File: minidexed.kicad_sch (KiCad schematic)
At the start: 50 parts, among them J1 AudioJack3, J2 AudioJack3, J3 AudioJack3, J4 AudioJack3, J5 Raspberry_Pi_2_3, SW1 SW_Push, SW2 SW_Push, SW3 SW_Push, SW4 Encoder, U1 A3.3V ME6211C33, U2 D3.3V ME6211C33, U3 74HCT14, U4 PCM5102, U5 6N138

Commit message: pre-tracks
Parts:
- removed C11, C12: 10, symbol Device:C
- removed C14, C15, C6: 0.1, symbol Device:C
- removed D1: 1N4148, Diode_THT:D_DO-35_SOD27_P7.62mm_Horizontal, symbol Diode:1N4148
- removed J1, J3: AudioJack3, symbol Connector:AudioJack3
- removed R6: 220, symbol Device:R
- removed R7: 3K3, symbol Device:R
- removed U2: D3.3V ME6211C33, Package_TO_SOT_SMD:TSOT-23-5, symbol Regulator_Linear:ADP7142AUJZ
- removed U5: 6N138, symbol Isolator:6N138
- added C13: 10uf, Capacitor_SMD:C_0805_2012Metric_Pad1.18x1.45mm_HandSolder, symbol Device:C
- added C7, C9: 100nf, Capacitor_SMD:C_0805_2012Metric_Pad1.18x1.45mm_HandSolder, symbol Device:C
- added D1: 1N4148WS, Diode_SMD:D_SOD-323, symbol Diode:1N4148WS
- added H1, H2, H3: MountingHole, MountingHole:MountingHole_2.7mm_M2.5, symbol Mechanical:MountingHole
- added J4: MIDI Thru, sparkfun 3.5mm:sparkfun_3.5mm_trs, symbol Connector:AudioJack3
- added J5: MIDI Out, sparkfun 3.5mm:sparkfun_3.5mm_trs, symbol Connector:AudioJack3
- added J6: GND TP, Connector_PinHeader_2.54mm:PinHeader_1x02_P2.54mm_Vertical, symbol Connector:Conn_01x02_Male
- added R12: 470, Resistor_SMD:R_1206_3216Metric_Pad1.30x1.75mm_HandSolder, symbol Device:R
- added TP5: 5V Analog DAC, TestPoint:TestPoint_Pad_D1.0mm, symbol Connector:TestPoint
- added TP6: 3.3V Analog DAC, TestPoint:TestPoint_Pad_D1.0mm, symbol Connector:TestPoint
- added TP8: 3.3V Digital DAC, TestPoint:TestPoint_Pad_D1.0mm, symbol Connector:TestPoint
- added U4: H11L1, Package_SO:TSOP-6_1.65x3.05mm_P0.95mm, symbol Isolator:H11L1
- C1, C5: value 0.1 -> 100nf; footprint (none) -> Capacitor_SMD:C_0805_2012Metric_Pad1.18x1.45mm_HandSolder; LCSC (none) -> C472810
- C10: value 10n -> 10uf; footprint (none) -> Capacitor_SMD:C_0805_2012Metric_Pad1.18x1.45mm_HandSolder; LCSC (none) -> C111662
- C11: renamed from C17; footprint (none) -> Capacitor_SMD:C_0805_2012Metric_Pad1.18x1.45mm_HandSolder; LCSC (none) -> C77455
- C12: renamed from C18; footprint (none) -> Capacitor_SMD:C_0805_2012Metric_Pad1.18x1.45mm_HandSolder; LCSC (none) -> C77455
- C14: renamed from C13; value 2.2 -> 2.2nf; footprint (none) -> Capacitor_SMD:C_0805_2012Metric_Pad1.18x1.45mm_HandSolder; LCSC (none) -> C395967
- C15: renamed from C16; value 2.2 -> 2.2nf; footprint (none) -> Capacitor_SMD:C_0805_2012Metric_Pad1.18x1.45mm_HandSolder; LCSC (none) -> C395967
- C16: renamed from C7; value 10n -> 0.1uf; footprint (none) -> Capacitor_SMD:C_0805_2012Metric_Pad1.18x1.45mm_HandSolder
- C2: value 0.1 -> 10uf; footprint (none) -> Capacitor_SMD:C_0805_2012Metric_Pad1.18x1.45mm_HandSolder; LCSC (none) -> C111662
- C3: value 10 -> 100nf; footprint (none) -> Capacitor_SMD:C_0805_2012Metric_Pad1.18x1.45mm_HandSolder; LCSC (none) -> C472810
- C4: value 10 -> 10uf; footprint (none) -> Capacitor_SMD:C_0805_2012Metric_Pad1.18x1.45mm_HandSolder; LCSC (none) -> C111662
- C6: renamed from C8; value 2.2 -> 2.2uf; footprint (none) -> Capacitor_SMD:C_0805_2012Metric_Pad1.18x1.45mm_HandSolder; LCSC (none) -> C6119894
- C8: renamed from C9; value 2.2 -> 2.2uf; footprint (none) -> Capacitor_SMD:C_0805_2012Metric_Pad1.18x1.45mm_HandSolder; LCSC (none) -> C6119894
- J1: renamed from J4; value AudioJack3 -> Audio Out; footprint (none) -> sparkfun 3.5mm:sparkfun_3.5mm_trs
- J2: value AudioJack3 -> MIDI In; footprint (none) -> sparkfun 3.5mm:sparkfun_3.5mm_trs
- J3: renamed from J5; footprint (none) -> raspberry-pi_rpi_hat:raspberry-pi_rpi_hat
- R1: renamed from R2; footprint (none) -> Resistor_SMD:R_1206_3216Metric_Pad1.30x1.75mm_HandSolder; LCSC (none) -> C104814
- R10: renamed from R4; footprint (none) -> Resistor_SMD:R_1206_3216Metric_Pad1.30x1.75mm_HandSolder; LCSC (none) -> C872616
- R11: renamed from R5; footprint (none) -> Resistor_SMD:R_1206_3216Metric_Pad1.30x1.75mm_HandSolder; LCSC (none) -> C872616
- R13: renamed from R8; footprint (none) -> Resistor_SMD:R_1206_3216Metric_Pad1.30x1.75mm_HandSolder; LCSC (none) -> C872616
- R14: renamed from R9; footprint (none) -> Resistor_SMD:R_1206_3216Metric_Pad1.30x1.75mm_HandSolder; LCSC (none) -> C872616
- R2: renamed from R10; footprint (none) -> Resistor_SMD:R_1206_3216Metric_Pad1.30x1.75mm_HandSolder; LCSC (none) -> C237143
- R3: renamed from R11; footprint (none) -> Resistor_SMD:R_1206_3216Metric_Pad1.30x1.75mm_HandSolder; LCSC (none) -> C237143
- R4: renamed from R3; footprint (none) -> Resistor_SMD:R_1206_3216Metric_Pad1.30x1.75mm_HandSolder; LCSC (none) -> C104814
- R5: renamed from R12; footprint (none) -> Resistor_SMD:R_1206_3216Metric_Pad1.30x1.75mm_HandSolder; LCSC (none) -> C237143
- R6: renamed from R1; footprint (none) -> Resistor_SMD:R_1206_3216Metric_Pad1.30x1.75mm_HandSolder; LCSC (none) -> C872616
- R7: renamed from R13; footprint (none) -> Resistor_SMD:R_1206_3216Metric_Pad1.30x1.75mm_HandSolder; LCSC (none) -> C912903
- R8: renamed from R14; footprint (none) -> Resistor_SMD:R_1206_3216Metric_Pad1.30x1.75mm_HandSolder; LCSC (none) -> C912903
- R9: renamed from R15; footprint (none) -> Resistor_SMD:R_1206_3216Metric_Pad1.30x1.75mm_HandSolder; LCSC (none) -> C912903
- RV1: value R_Potentiometer -> 10k; footprint (none) -> Potentiometer_THT:Potentiometer_Runtron_RM-065_Vertical
- SW1: renamed from SW4; footprint (none) -> Rotary_Encoder:RotaryEncoder_Alps_EC11E-Switch_Vertical_H20mm
- SW2: renamed from SW1; value SW_Push -> B1; footprint (none) -> Button_Switch_Keyboard:SW_Cherry_MX_1.00u_PCB
- SW3: renamed from SW2; value SW_Push -> B2; footprint (none) -> Button_Switch_Keyboard:SW_Cherry_MX_1.00u_PCB
- SW4: renamed from SW3; value SW_Push -> B3; footprint (none) -> Button_Switch_Keyboard:SW_Cherry_MX_1.00u_PCB
- U1: LCSC (none) -> C82942
- U2: renamed from U4; LCSC (none) -> C107671
- U3: footprint (none) -> Package_SO:TSSOP-14_4.4x3.6mm_P0.4mm; LCSC (none) -> C133639
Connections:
- net DAC_D_3V3 is gone; now on net +3.3V: C4.1, U2.17 (XSMT), U2.20 (DVDD)
- net +3.3V: now also C5.1, R12.1, TP8.1, U4.6; no longer C10.1
- net +5V: now also TP5.1; no longer C2.1
- net DAC_A_3V3: now also C10.1, C2.1, C7.1, TP6.1; no longer C5.1
- net GND: now also C6.2, J1.1 (S), U2.3 (CPGND), C13.2, C7.2, C9.2, J4.1 (S), J5.1 (S), J6.1 (Pin_1), J6.2 (Pin_2), U4.5; no longer J1.S, J2.S
- net MIDI_RX: now also R12.2, U4.4
- net at R13.1: now also J4.2 (R); no longer J2.R
- net at R10.1: now also J4.5 (T); no longer J2.T
- net at C14.1, R1.2: now also J1.5 (T); no longer J1.T
- net at R14.1: now also J5.2 (R)
- net at R6.2: now also D1.1 (K), U4.1
- net at U2.18 (LDOO): now also C13.1, C9.1
- net at R6.1: now also J2.2 (R)
- net at C15.1, R4.2: now also J1.2 (R); no longer J1.R
- net at R11.1: now also J5.5 (T)
- new net: D1.2 (A), J2.5 (T), U4.2
- no-connect marks 20 -> 19
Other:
- removed sheet DAC
- removed sheet MIDI IO
- note added: "BUTTONS"
- note added: "DAC"
- note added: "ENCODER"
- note added: "I don't think an optocoupler needs a bypass cap?"
- note added: "Is this overkill using a regulator when we already have 3.3V available?"
- note added: "MIDI"
- note added: "RPI"
- note removed: "INTERFACE"
- note removed: "MIDI IN"
- note removed: "MIDI OUT"
- note removed: "MIDI THRU"
- note removed: "Questions: - Analog vs digital ground"
- moved on the sheet: C1, C11, C12, C14, C15, C16, C6, C8, DS1, J3, R1, R10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

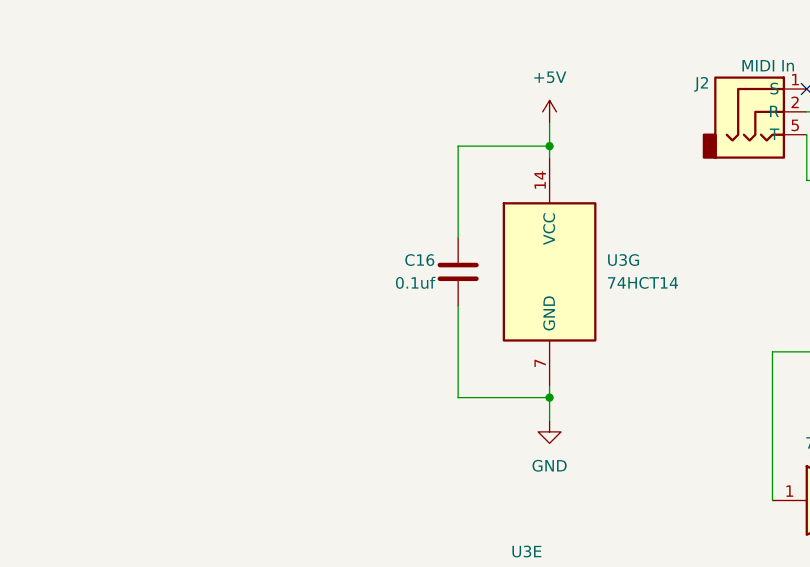
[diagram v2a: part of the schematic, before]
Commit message: update opto footprint
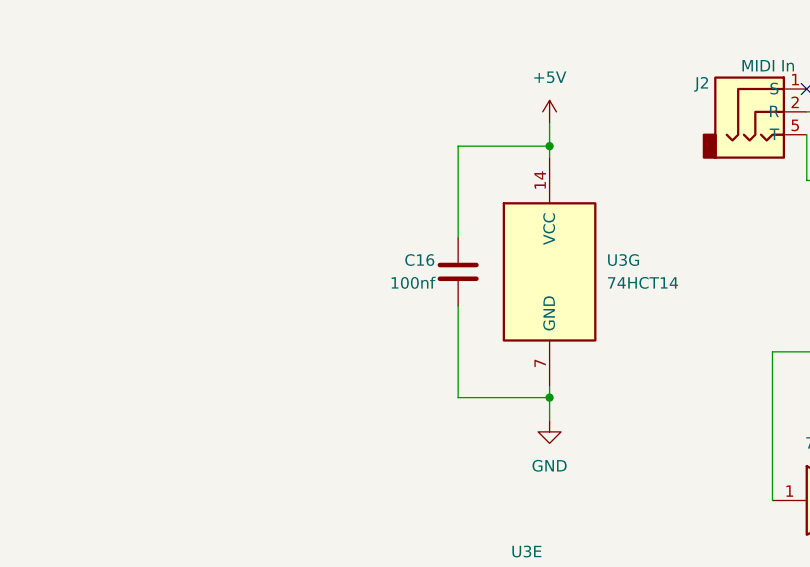
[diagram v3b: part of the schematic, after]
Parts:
- C16: value 0.1uf -> 100nf; LCSC (none) -> C472810
- R2, R3, R5: LCSC C237143 -> C2073539
- U3: footprint Package_SO:TSSOP-14_4.4x3.6mm_P0.4mm -> Package_SO:TSSOP-14_4.4x5mm_P0.65mm
- U4: footprint Package_SO:TSOP-6_1.65x3.05mm_P0.95mm -> SOP-6_6.5x7.12mm_P2.54mm:SOP-6_6.5x7.12mm_P2.54mm
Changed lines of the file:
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@@
     (property "Reference" "U4" (id 0) (at 420.37 242.57 0))
     (property "Value" "H11L1" (id 1) (at 421.64 245.11 0))
-    (property "Footprint" "Package_SO:TSOP-6_1.65x3.05mm_P0.95mm" (id 2) (at 410.464 240.03 0)
+    (property "Footprint" "SOP-6_6.5x7.12mm_P2.54mm:SOP-6_6.5x7.12mm_P2.54mm" (id 2) (at 410.464 240.03 0)
       (effects (font (size 1.27 1.27)) hide)
     )
@@
     (property "Reference" "U3" (id 0) (at 408.94 271.78 0))
     (property "Value" "74HCT14" (id 1) (at 408.94 274.32 0))
-    (property "Footprint" "Package_SO:TSSOP-14_4.4x3.6mm_P0.4mm" (id 2) (at 408.94 280.67 0)
+    (property "Footprint" "Package_SO:TSSOP-14_4.4x5mm_P0.65mm" (id 2) (at 408.94 280.67 0)
       (effects (font (size 1.27 1.27)) hide)
     )
@@
       (effects (font (size 1.27 1.27)) hide)
     )
-    (property "LCSC" "C237143" (id 4) (at 239.395 72.39 0)
+    (property "LCSC" "C2073539" (id 4) (at 239.395 72.39 0)
       (effects (font (size 1.27 1.27)) hide)
     )
@@
     (property "Reference" "U3" (id 0) (at 388.62 271.78 0))
     (property "Value" "74HCT14" (id 1) (at 388.62 274.32 0))
-    (property "Footprint" "Package_SO:TSSOP-14_4.4x3.6mm_P0.4mm" (id 2) (at 388.62 280.67 0)
+    (property "Footprint" "Package_SO:TSSOP-14_4.4x5mm_P0.65mm" (id 2) (at 388.62 280.67 0)
       (effects (font (size 1.27 1.27)) hide)
     )
@@
       (effects (font (size 1.27 1.27)) hide)
     )
-    (property "LCSC" "C237143" (id 4) (at 273.685 78.74 0)
+    (property "LCSC" "C2073539" (id 4) (at 273.685 78.74 0)
       (effects (font (size 1.27 1.27)) hide)
     )
@@
       (effects (font (size 1.27 1.27)) hide)
     )
-    (property "LCSC" "C237143" (id 4) (at 239.395 96.52 0)
+    (property "LCSC" "C2073539" (id 4) (at 239.395 96.52 0)
       (effects (font (size 1.27 1.27)) hide)
     )
@@
       (effects (font (size 1.27 1.27)) (justify left))
     )
-    (property "Footprint" "Package_SO:TSSOP-14_4.4x3.6mm_P0.4mm" (id 2) (at 356.235 255.27 0)
+    (property "Footprint" "Package_SO:TSSOP-14_4.4x5mm_P0.65mm" (id 2) (at 356.235 255.27 0)
       (effects (font (size 1.27 1.27)) hide)
     )
@@
     (property "Reference" "U3" (id 0) (at 353.695 301.625 0))
     (property "Value" "74HCT14" (id 1) (at 353.695 304.165 0))
-    (property "Footprint" "Package_SO:TSSOP-14_4.4x3.6mm_P0.4mm" (id 2) (at 353.695 310.515 0)
+    (property "Footprint" "Package_SO:TSSOP-14_4.4x5mm_P0.65mm" (id 2) (at 353.695 310.515 0)
       (effects (font (size 1.27 1.27)) hide)
     )
@@
       (effects (font (size 1.27 1.27)) (justify left))
     )
-    (property "Value" "0.1uf" (id 1) (at 343.535 256.54 0)
+    (property "Value" "100nf" (id 1) (at 343.535 256.54 0)
       (effects (font (size 1.27 1.27)) (justify left))
     )
@@
     )
     (property "Datasheet" "~" (id 3) (at 346.075 255.27 0)
+      (effects (font (size 1.27 1.27)) hide)
+    )
+    (property "LCSC" "C472810" (id 4) (at 346.075 255.27 0)
       (effects (font (size 1.27 1.27)) hide)
     )
@@
     (property "Reference" "U3" (id 0) (at 388.62 294.64 0))
     (property "Value" "74HCT14" (id 1) (at 388.62 297.18 0))
-    (property "Footprint" "Package_SO:TSSOP-14_4.4x3.6mm_P0.4mm" (id 2) (at 388.62 303.53 0)
+    (property "Footprint" "Package_SO:TSSOP-14_4.4x5mm_P0.65mm" (id 2) (at 388.62 303.53 0)
       (effects (font (size 1.27 1.27)) hide)
     )
@@
     (property "Reference" "U3" (id 0) (at 353.695 286.385 0))
     (property "Value" "74HCT14" (id 1) (at 353.695 288.925 0))
-    (property "Footprint" "Package_SO:TSSOP-14_4.4x3.6mm_P0.4mm" (id 2) (at 353.695 295.275 0)
+    (property "Footprint" "Package_SO:TSSOP-14_4.4x5mm_P0.65mm" (id 2) (at 353.695 295.275 0)
       (effects (font (size 1.27 1.27)) hide)
     )
@@
     (property "Reference" "U3" (id 0) (at 408.94 294.64 0))
     (property "Value" "74HCT14" (id 1) (at 408.94 297.18 0))
-    (property "Footprint" "Package_SO:TSSOP-14_4.4x3.6mm_P0.4mm" (id 2) (at 408.94 303.53 0)
+    (property "Footprint" "Package_SO:TSSOP-14_4.4x5mm_P0.65mm" (id 2) (at 408.94 303.53 0)
       (effects (font (size 1.27 1.27)) hide)
     )
@@
     )
     (path "/bc30b584-f4e9-4a30-a37e-c076b2785d61"
-      (reference "C16") (unit 1) (value "0.1uf") (footprint "Capacitor_SMD:C_0805_2012Metric_Pad1.18x1.45mm_HandSolder")
+      (reference "C16") (unit 1) (value "100nf") (footprint "Capacitor_SMD:C_0805_2012Metric_Pad1.18x1.45mm_HandSolder")
     )
     (path "/a4fe2f9d-af8f-418b-b5d5-bc5fa9ea4d2b"
@@
     )
     (path "/4cb0ff7d-e882-4725-b871-5423066483c3"
-      (reference "U3") (unit 1) (value "74HCT14") (footprint "Package_SO:TSSOP-14_4.4x3.6mm_P0.4mm")
+      (reference "U3") (unit 1) (value "74HCT14") (footprint "Package_SO:TSSOP-14_4.4x5mm_P0.65mm")
     )
     (path "/0ecdddc5-bd56-46ad-a0b3-dd9fd99f99be"
-      (reference "U3") (unit 2) (value "74HCT14") (footprint "Package_SO:TSSOP-14_4.4x3.6mm_P0.4mm")
+      (reference "U3") (unit 2) (value "74HCT14") (footprint "Package_SO:TSSOP-14_4.4x5mm_P0.65mm")
     )
     (path "/e420f296-c430-4673-841d-989f25602224"
-      (reference "U3") (unit 3) (value "74HCT14") (footprint "Package_SO:TSSOP-14_4.4x3.6mm_P0.4mm")
+      (reference "U3") (unit 3) (value "74HCT14") (footprint "Package_SO:TSSOP-14_4.4x5mm_P0.65mm")
     )
     (path "/f247ef7a-acae-496d-a62b-d2c3dff2bde5"
-      (reference "U3") (unit 4) (value "74HCT14") (footprint "Package_SO:TSSOP-14_4.4x3.6mm_P0.4mm")
+      (reference "U3") (unit 4) (value "74HCT14") (footprint "Package_SO:TSSOP-14_4.4x5mm_P0.65mm")
     )
     (path "/ed460fdb-e9f6-4d7d-9b41-cecf19cf1c82"
-      (reference "U3") (unit 5) (value "74HCT14") (footprint "Package_SO:TSSOP-14_4.4x3.6mm_P0.4mm")
+      (reference "U3") (unit 5) (value "74HCT14") (footprint "Package_SO:TSSOP-14_4.4x5mm_P0.65mm")
     )
     (path "/bb939305-fbe1-41ba-a4d2-2bcf5669accd"
-      (reference "U3") (unit 6) (value "74HCT14") (footprint "Package_SO:TSSOP-14_4.4x3.6mm_P0.4mm")
+      (reference "U3") (unit 6) (value "74HCT14") (footprint "Package_SO:TSSOP-14_4.4x5mm_P0.65mm")
     )
     (path "/b8c7edcc-33af-4c79-a0bb-d37f3ab6ee7d"
-      (reference "U3") (unit 7) (value "74HCT14") (footprint "Package_SO:TSSOP-14_4.4x3.6mm_P0.4mm")
+      (reference "U3") (unit 7) (value "74HCT14") (footprint "Package_SO:TSSOP-14_4.4x5mm_P0.65mm")
     )
     (path "/01d5d82e-8b84-430e-81cb-78886e1a70e6"
-      (reference "U4") (unit 1) (value "H11L1") (footprint "Package_SO:TSOP-6_1.65x3.05mm_P0.95mm")
-    )
-  )
+      (reference "U4") (unit 1) (value "H11L1") (footprint "SOP-6_6.5x7.12mm_P2.54mm:SOP-6_6.5x7.12mm_P2.54mm")
+    )
+  )

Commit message: add acrylic faceplates
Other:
- note added: "TODO: - Add holes for 3.5mm jack braces - Move 3.5mm jacks higher"
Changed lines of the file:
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@@
+    (effects (font (size 1.27 1.27)) (justify left bottom))
+  )
+  (text "TODO:\n- Add holes for 3.5mm jack braces\n- Move 3.5mm jacks higher"
+    (at 461.518 56.134 0)
     (effects (font (size 1.27 1.27)) (justify left bottom))
   )
